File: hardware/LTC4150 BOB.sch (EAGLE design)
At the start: 23 parts, among them U1 LTC4150

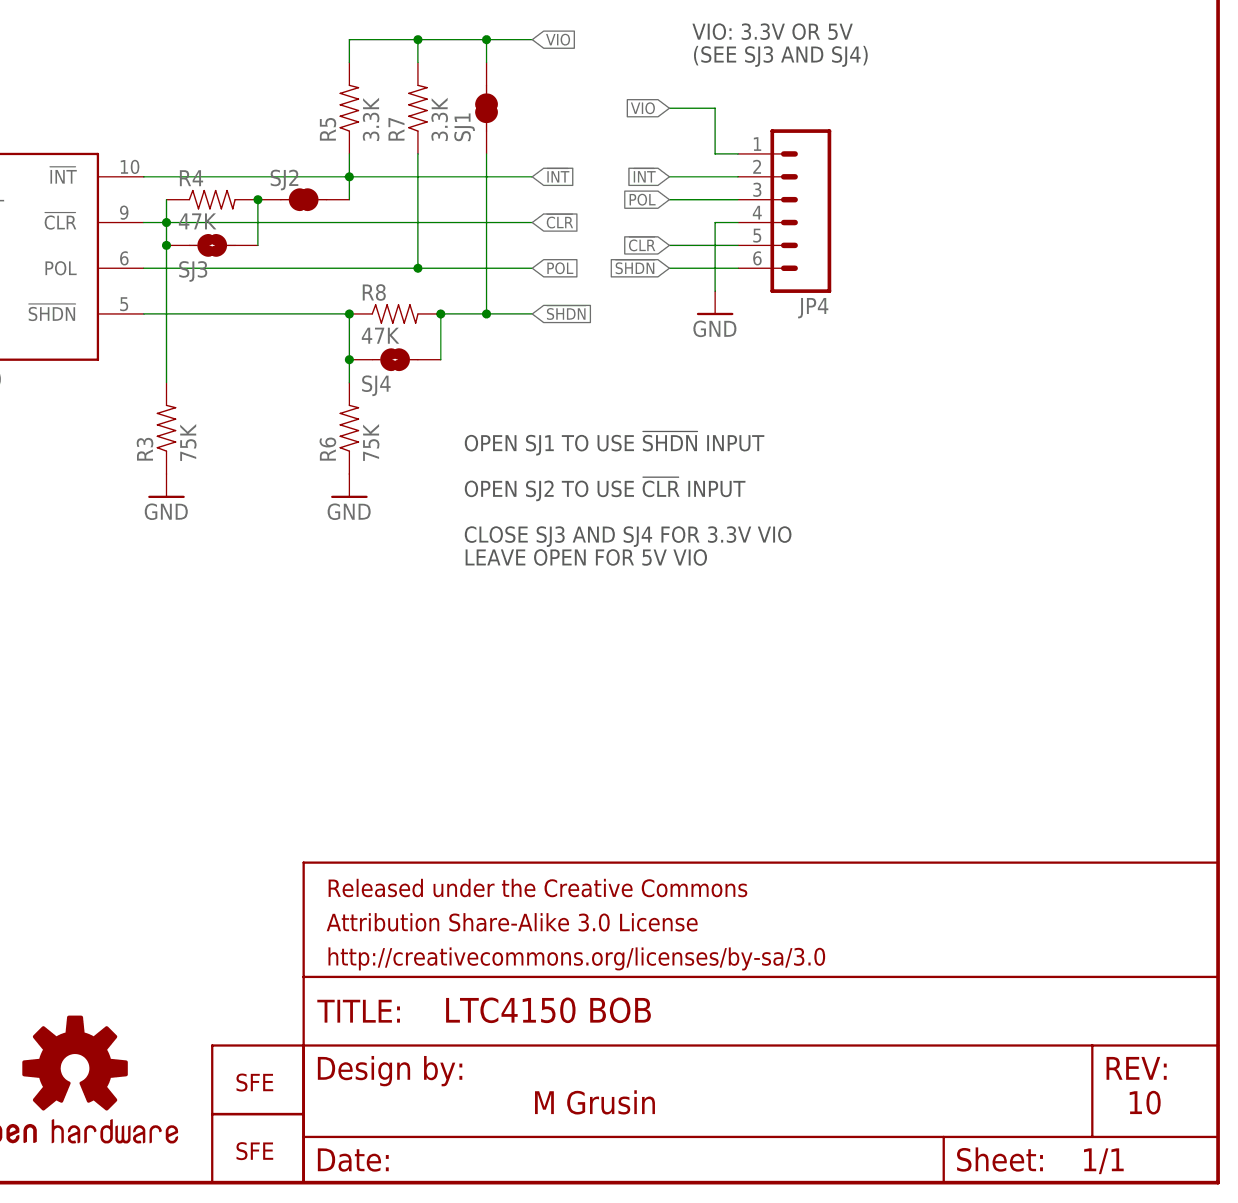
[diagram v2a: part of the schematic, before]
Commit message: fixed resistor layout for 5V operation
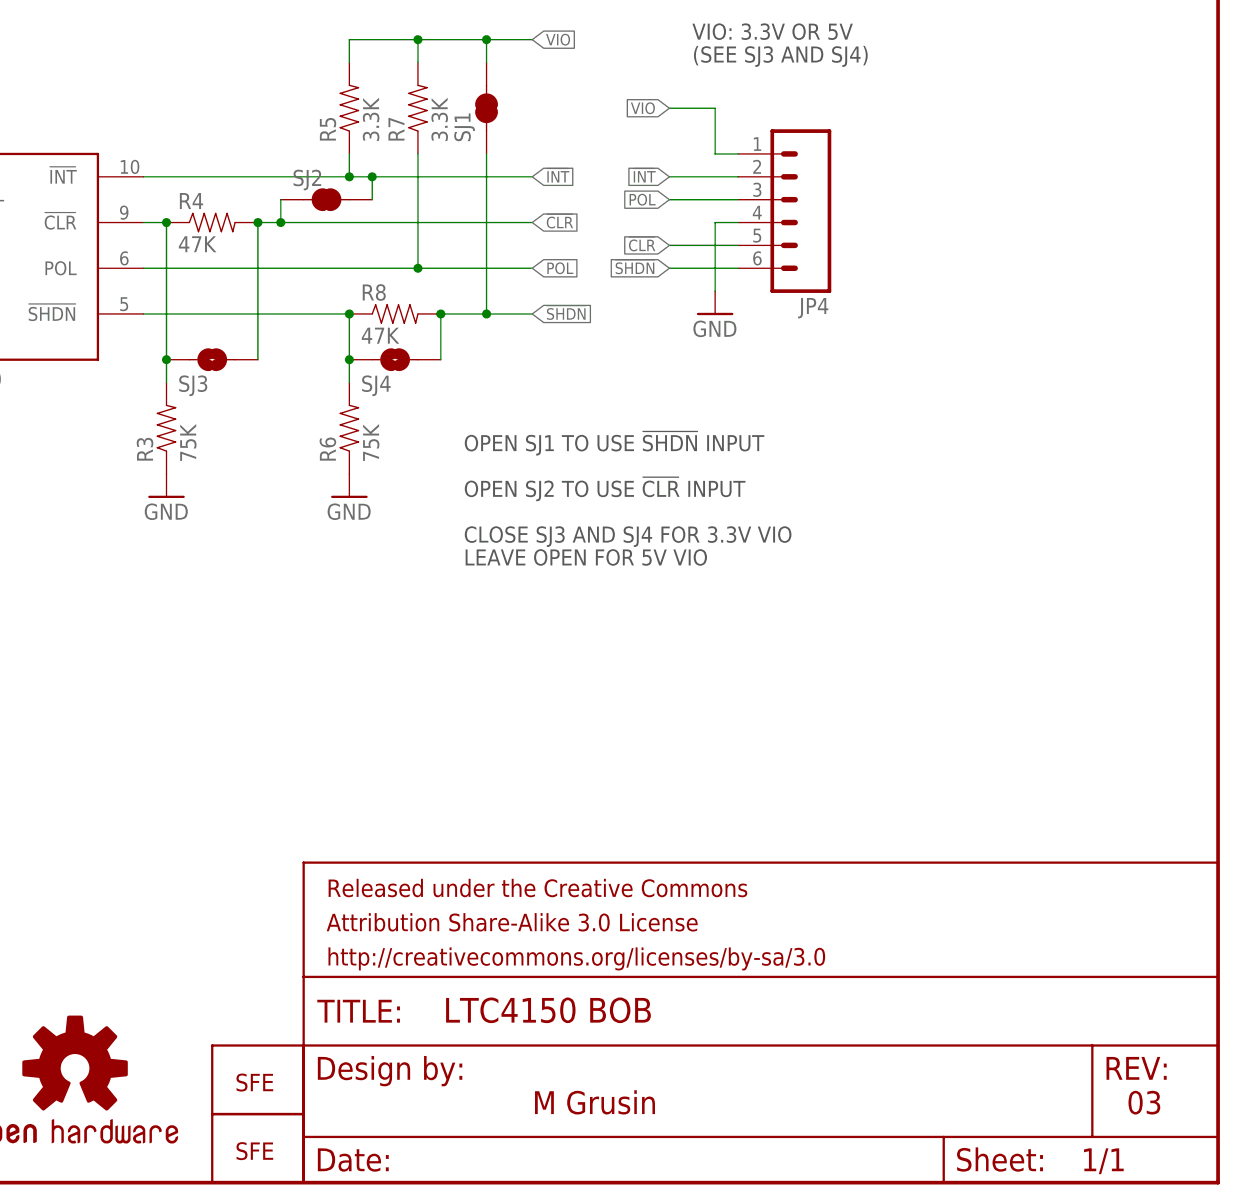
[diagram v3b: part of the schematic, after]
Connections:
- net !CLR!: now also R4.2, SJ2.1, SJ3.2; no longer R3.2, R4.1, SJ3.1, U1.!CLR!
- net N$1: now also R3.2, R4.1, SJ3.1, U1.!CLR!; no longer R4.2, SJ2.1, SJ3.2
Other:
- note added: "03"
- note removed: "10"
- moved on the sheet: R4, SJ2, SJ3
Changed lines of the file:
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@@
 <plain>
 <text x="172.72" y="7.62" size="2.54" layer="94">M Grusin</text>
-<text x="238.76" y="7.62" size="2.54" layer="94">10</text>
+<text x="238.76" y="7.62" size="2.54" layer="94">03</text>
 <text x="165.1" y="71.12" size="1.778" layer="97">CLOSE SJ3 AND SJ4 FOR 3.3V VIO</text>
 <text x="165.1" y="81.28" size="1.778" layer="97">OPEN SJ1 TO USE !SHDN! INPUT</text>
@@
 <text x="165.1" y="134.62" size="1.778" layer="97">5859 !INT!S = 1 Ah</text>
 <text x="165.1" y="76.2" size="1.778" layer="97">OPEN SJ2 TO USE !CLR! INPUT</text>
-<rectangle x1="146.558" y1="108.712" x2="148.082" y2="109.728" layer="94"/>
+<rectangle x1="149.098" y1="108.712" x2="150.622" y2="109.728" layer="94"/>
 <rectangle x1="167.132" y1="118.364" x2="168.148" y2="120.142" layer="94"/>
 <text x="55.88" y="139.7" size="1.778" layer="97">0.05 OHMS = 1.0A MAX</text>
@@
 <instance part="R6" gate="G$1" x="152.4" y="83.82" rot="R90"/>
 <instance part="R7" gate="G$1" x="160.02" y="119.38" rot="R90"/>
-<instance part="R4" gate="G$1" x="137.16" y="109.22"/>
+<instance part="R4" gate="G$1" x="137.16" y="106.68"/>
 <instance part="GND1" gate="1" x="132.08" y="76.2"/>
 <instance part="GND2" gate="1" x="152.4" y="76.2"/>
@@
 <instance part="LOGO3" gate="G$1" x="139.7" y="2.54"/>
 <instance part="LOGO1" gate="G$1" x="121.92" y="12.7"/>
-<instance part="SJ3" gate="1" x="137.16" y="104.14" smashed="yes" rot="MR180">
-<attribute name="NAME" x="133.35" y="102.362" size="1.778" layer="95" rot="MR180"/>
-<attribute name="VALUE" x="134.62" y="109.22" size="1.778" layer="96" rot="MR180"/>
+<instance part="SJ3" gate="1" x="137.16" y="91.44" smashed="yes" rot="MR180">
+<attribute name="NAME" x="133.35" y="89.662" size="1.778" layer="95" rot="MR180"/>
+<attribute name="VALUE" x="134.62" y="96.52" size="1.778" layer="96" rot="MR180"/>
 </instance>
 <instance part="SJ1" gate="1" x="167.64" y="119.38" smashed="yes" rot="MR270">
@@
 </instance>
 <instance part="LOGO2" gate="G$1" x="139.7" y="10.16"/>
-<instance part="SJ2" gate="1" x="147.32" y="109.22" smashed="yes" rot="MR180">
-<attribute name="NAME" x="143.51" y="112.522" size="1.778" layer="95" rot="MR180"/>
-<attribute name="VALUE" x="144.78" y="114.3" size="1.778" layer="96" rot="MR180"/>
+<instance part="SJ2" gate="1" x="149.86" y="109.22" smashed="yes" rot="MR180">
+<attribute name="NAME" x="146.05" y="112.522" size="1.778" layer="95" rot="MR180"/>
+<attribute name="VALUE" x="147.32" y="114.3" size="1.778" layer="96" rot="MR180"/>
 </instance>
 <instance part="R2" gate="G$1" x="71.12" y="114.3"/>
@@
 <pinref part="U1" gate="G$1" pin="!INT!"/>
 <wire x1="129.54" y1="111.76" x2="152.4" y2="111.76" width="0.1524" layer="91"/>
-<wire x1="152.4" y1="111.76" x2="172.72" y2="111.76" width="0.1524" layer="91"/>
+<wire x1="152.4" y1="111.76" x2="154.94" y2="111.76" width="0.1524" layer="91"/>
 <pinref part="R5" gate="G$1" pin="1"/>
+<wire x1="154.94" y1="111.76" x2="172.72" y2="111.76" width="0.1524" layer="91"/>
 <wire x1="152.4" y1="114.3" x2="152.4" y2="111.76" width="0.1524" layer="91"/>
 <junction x="152.4" y="111.76"/>
 <label x="172.72" y="111.76" size="1.27" layer="95" xref="yes"/>
 <pinref part="SJ2" gate="1" pin="2"/>
-<wire x1="152.4" y1="109.22" x2="152.4" y2="111.76" width="0.1524" layer="91"/>
+<wire x1="154.94" y1="109.22" x2="154.94" y2="111.76" width="0.1524" layer="91"/>
+<junction x="154.94" y="111.76"/>
 </segment>
 <segment>
@@
 <wire x1="152.4" y1="88.9" x2="152.4" y2="91.44" width="0.1524" layer="91"/>
 <junction x="152.4" y="91.44"/>
-</segment>
-</net>
-<net name="!CLR!" class="0">
-<segment>
-<pinref part="U1" gate="G$1" pin="!CLR!"/>
-<wire x1="132.08" y1="106.68" x2="129.54" y2="106.68" width="0.1524" layer="91"/>
-<wire x1="132.08" y1="106.68" x2="172.72" y2="106.68" width="0.1524" layer="91"/>
-<junction x="132.08" y="106.68"/>
-<pinref part="R3" gate="G$1" pin="2"/>
-<wire x1="132.08" y1="88.9" x2="132.08" y2="104.14" width="0.1524" layer="91"/>
-<pinref part="R4" gate="G$1" pin="1"/>
-<wire x1="132.08" y1="104.14" x2="132.08" y2="106.68" width="0.1524" layer="91"/>
-<wire x1="132.08" y1="109.22" x2="132.08" y2="106.68" width="0.1524" layer="91"/>
-<label x="172.72" y="106.68" size="1.27" layer="95" xref="yes"/>
-<pinref part="SJ3" gate="1" pin="1"/>
-<junction x="132.08" y="104.14"/>
-</segment>
-<segment>
-<pinref part="JP4" gate="G$1" pin="5"/>
-<wire x1="195.58" y1="104.14" x2="187.96" y2="104.14" width="0.1524" layer="91"/>
-<label x="187.96" y="104.14" size="1.27" layer="95" rot="R180" xref="yes"/>
 </segment>
 </net>
@@
 </segment>
 </net>
-<net name="N$1" class="0">
+<net name="!CLR!" class="0">
 <segment>
 <pinref part="SJ3" gate="1" pin="2"/>
 <pinref part="R4" gate="G$1" pin="2"/>
-<junction x="142.24" y="109.22"/>
+<junction x="142.24" y="106.68"/>
 <pinref part="SJ2" gate="1" pin="1"/>
-<wire x1="142.24" y1="109.22" x2="142.24" y2="104.14" width="0.1524" layer="91"/>
-</segment>
-</net>
+<wire x1="142.24" y1="106.68" x2="142.24" y2="91.44" width="0.1524" layer="91"/>
+<wire x1="142.24" y1="106.68" x2="144.78" y2="106.68" width="0.1524" layer="91"/>
+<wire x1="144.78" y1="106.68" x2="172.72" y2="106.68" width="0.1524" layer="91"/>
+<wire x1="144.78" y1="109.22" x2="144.78" y2="106.68" width="0.1524" layer="91"/>
+<junction x="144.78" y="106.68"/>
+<label x="172.72" y="106.68" size="1.27" layer="95" xref="yes"/>
+</segment>
+<segment>
+<pinref part="JP4" gate="G$1" pin="5"/>
+<wire x1="195.58" y1="104.14" x2="187.96" y2="104.14" width="0.1524" layer="91"/>
+<label x="187.96" y="104.14" size="1.27" layer="95" rot="R180" xref="yes"/>
+</segment>
+</net>
+<net name="N$1" class="0">
+<segment>
+<pinref part="R3" gate="G$1" pin="2"/>
+<pinref part="SJ3" gate="1" pin="1"/>
+<wire x1="132.08" y1="88.9" x2="132.08" y2="91.44" width="0.1524" layer="91"/>
+<pinref part="R4" gate="G$1" pin="1"/>
+<wire x1="132.08" y1="91.44" x2="132.08" y2="106.68" width="0.1524" layer="91"/>
+<junction x="132.08" y="91.44"/>
+<pinref part="U1" gate="G$1" pin="!CLR!"/>
+<wire x1="132.08" y1="106.68" x2="129.54" y2="106.68" width="0.1524" layer="91"/>
+<junction x="132.08" y="106.68"/>
+</segment>
+</net>

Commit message: Changed temp parts to SparkFun library variants
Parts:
- SJ1: device mike-temp:SOLDERJUMPERNC -> SparkFun-Passives:SOLDERJUMPERNC
- SJ3, SJ4: device mike-temp:SOLDERJUMPERNO -> SparkFun-Passives:SOLDERJUMPERNO
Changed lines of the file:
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@@
 <?xml version="1.0" encoding="utf-8"?>
 <!DOCTYPE eagle SYSTEM "eagle.dtd">
-<eagle version="6.4">
+<eagle version="6.5.0">
 <drawing>
 <settings>
@@
 <part name="LOGO3" library="SparkFun-Aesthetics" deviceset="LOGO-SFE" device="SK"/>
 <part name="LOGO1" library="SparkFun-Aesthetics" deviceset="OSHW-LOGO" device="S"/>
-<part name="SJ3" library="mike-temp" deviceset="SOLDERJUMPER" device="NO" value=""/>
-<part name="SJ1" library="mike-temp" deviceset="SOLDERJUMPER" device="NC" value=""/>
+<part name="SJ3" library="SparkFun-Passives" deviceset="SOLDERJUMPER" device="NO" value=""/>
+<part name="SJ1" library="SparkFun-Passives" deviceset="SOLDERJUMPER" device="NC" value=""/>
 <part name="LOGO2" library="SparkFun-Aesthetics" deviceset="LOGO-SFE" device="NW2"/>
 <part name="SJ2" library="SparkFun-Passives" deviceset="SOLDERJUMPER" device="NC" value=""/>
 <part name="R2" library="SparkFun-Passives" deviceset="RESISTOR" device="AXIAL-0.3" value="DNP"/>
-<part name="SJ4" library="mike-temp" deviceset="SOLDERJUMPER" device="NO" value=""/>
+<part name="SJ4" library="SparkFun-Passives" deviceset="SOLDERJUMPER" device="NO" value=""/>
 </parts>
 <sheets>
